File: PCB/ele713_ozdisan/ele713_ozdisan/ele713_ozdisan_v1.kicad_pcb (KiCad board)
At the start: 2 copper layers, 200 x 100 mm, 82 parts, among them J1 Conn_01x02_Pin, J2 Conn_01x02_Pin, J3 Conn_01x10, J4 Conn_01x10, Q1 FDD86110, Q2 FDD86110, Q5 PZT2222AT1G, Q6 PZT2907AT1G, T2 ELE713 Transformer, U1 2EDS8265H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

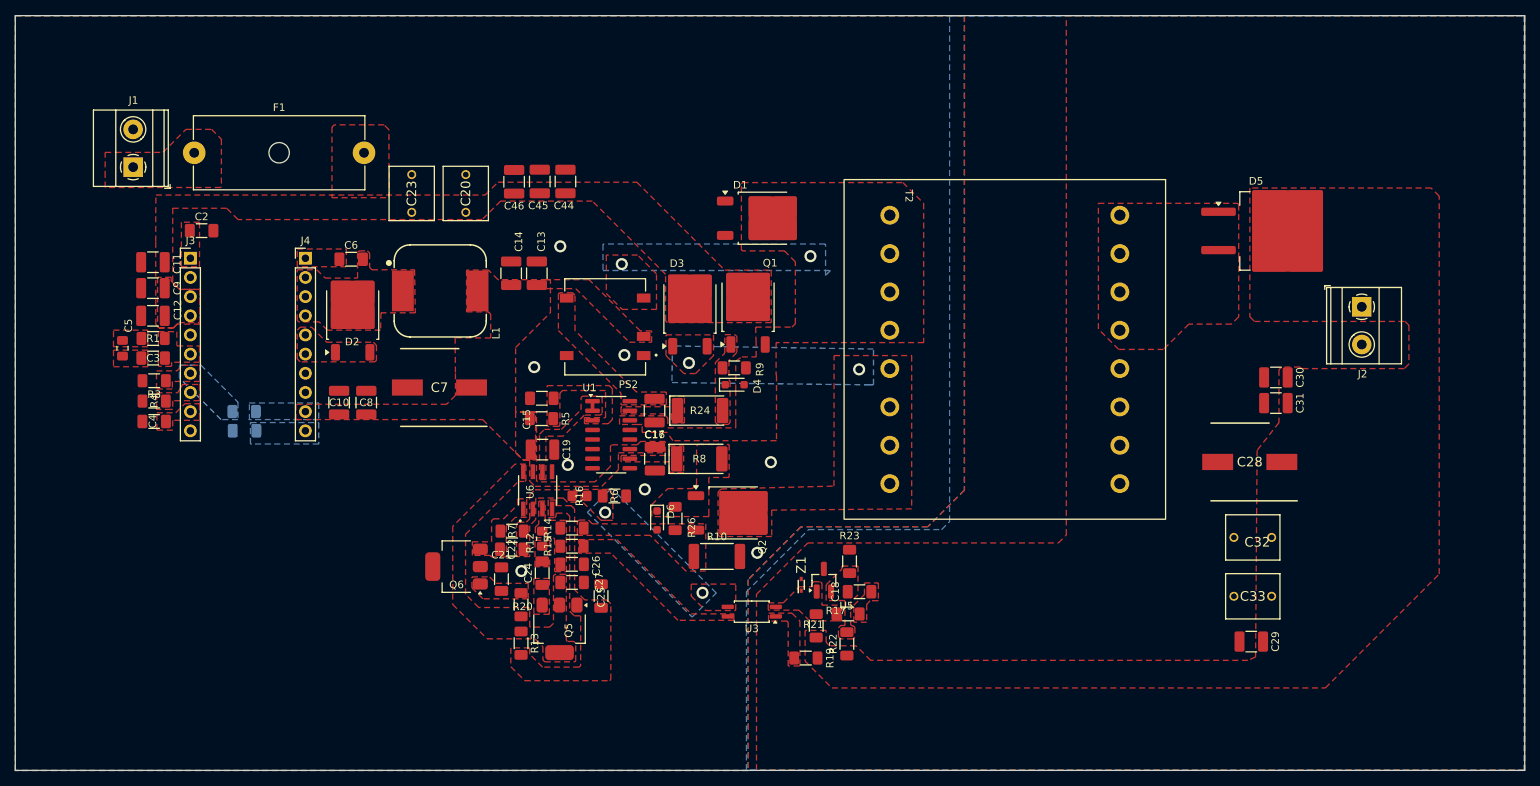
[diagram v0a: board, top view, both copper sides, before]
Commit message: PCB v1 ve v2 çizildi
Çok sancılı bir süreç, ilk PCB yi çizmek zormuş yıprandım. Neyse, v1 ve v2 çizildi. V2 basılacak olan şimdilik.
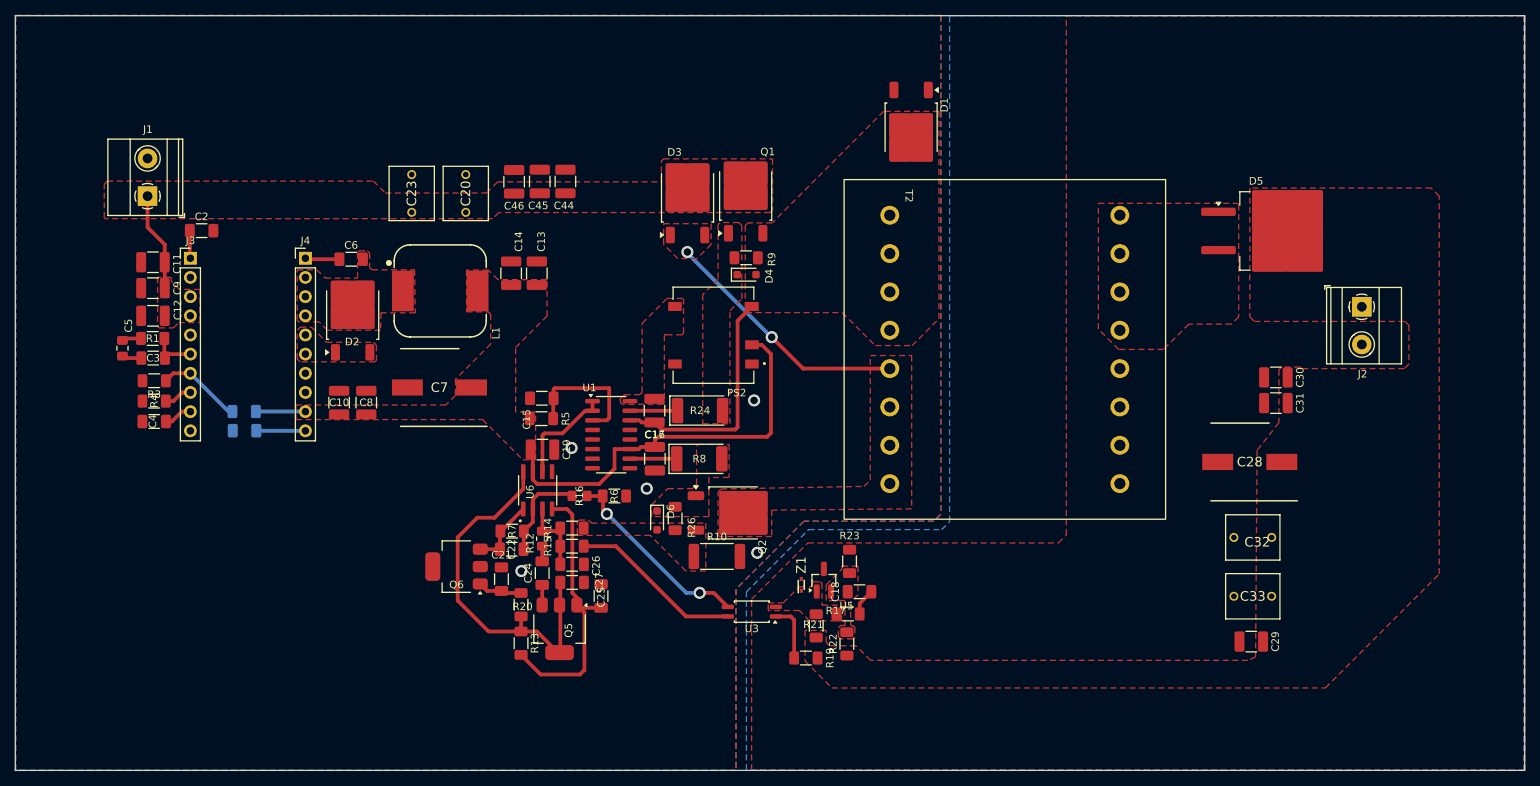
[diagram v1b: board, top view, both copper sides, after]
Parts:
- removed F1: Fuse, Fuse:Fuseholder_Cylinder-5x20mm_Schurter_0031_8201_Horizontal_Open
- moved D1 23.0 mm to (160.5, 56.1), turned to -90 degrees
- moved D3 14.7 mm to (130.8, 65.2)
- moved Q1 14.7 mm to (138.5, 65.0)
- moved D4 14.7 mm to (138.7, 75.5)
- moved R9 14.7 mm to (138.6, 73.3)
- moved PS2 14.4 mm to (134.3, 83.5)
- moved J1 4.30 mm to (59.3, 65.1)
- moved R1 0.06 mm to (60.0, 83.9)
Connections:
- J1 pad 1: VIN_UNPROTECTED -> VIN
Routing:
- net +12V: track 0.70 -> 61.8 mm
- net Net-(Q5-C): track 0.34 -> 49.7 mm
- net Net-(Q5-B): track 0.00 -> 37.3 mm
- net Net-(Q2-D): track 0.00 -> 33.3 mm
- net ISOGND: track 0.89 -> 31.7 mm, vias 2 -> 0
- net Net-(R16-Pad2): track 0.09 -> 25.8 mm
- net Net-(R15-Pad2): track 0.00 -> 22.9 mm
- net Net-(U1-VDDI): track 0.00 -> 17.6 mm
- net VIN: track 0.01 -> 13.1 mm
- net /PWM: track 1.27 -> 14.1 mm
- net Net-(U6-FB): track 0.00 -> 12.7 mm
- net /LM5576_7: track 0.00 -> 11.3 mm
- net Net-(U6-ISENSE): track 0.05 -> 10.2 mm
- net Net-(Q6-E): track 0.19 -> 9.27 mm
- net Net-(R19-Pad1): track 0.00 -> 7.67 mm
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- removed copper zone on B.Cu, net +12V
- removed copper zone on F.Cu, net /GATE_HIGH
- removed copper zone on F.Cu, net /GATE_LOW
- removed copper zone on F.Cu, net /LM5576_1
- removed copper zone on B.Cu, net /LM5576_11
- removed copper zone on F.Cu, net /LM5576_20
- removed copper zone on F.Cu, net /LM5576_6
- removed copper zone on B.Cu, net /LM5576_7
- removed copper zone on F.Cu, net /LM5576_7
- removed copper zone on F.Cu, net /LM5576_8
- removed copper zone on F.Cu, net /LM5576_9
- removed copper zone on F.Cu, net /PWM
- removed copper zone on B.Cu, net ISOGND
- removed copper zone on F.Cu, net Net-(C18-Pad1)
- removed copper zone on F.Cu, net Net-(C24-Pad2)
- removed copper zone on F.Cu, net Net-(C3-Pad2)
- removed copper zone on F.Cu, net Net-(C5-Pad1)
- removed copper zone on B.Cu, net Net-(Q2-D)
- removed copper zone on F.Cu, net Net-(Q5-B)
- removed copper zone on F.Cu, net Net-(Q5-C)
- removed copper zone on F.Cu, net Net-(Q5-E)
- removed copper zone on F.Cu, net Net-(Q6-B)
- removed copper zone on F.Cu, net Net-(Q6-E)
- removed copper zone on F.Cu, net Net-(R15-Pad2)
- removed copper zone on B.Cu, net Net-(R16-Pad2)
- removed copper zone on F.Cu, net Net-(R16-Pad2)
- removed copper zone on F.Cu, net Net-(R19-Pad1)
- removed copper zone on F.Cu, net Net-(U1-VDDI)
- removed copper zone on F.Cu, net Net-(U6-FB)
- removed copper zone on F.Cu, net Net-(U6-ISENSE)
- removed copper zone on F.Cu, net VIN_UNPROTECTED
